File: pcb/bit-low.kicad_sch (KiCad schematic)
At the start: 5 parts, among them Q1 2N7002b, Q2 2N7002b

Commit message: Bit low/high.
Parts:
- renumbered C5 to C23, Q1 to Q909, Q2 to Q910, R1 to R396, R2 to R397
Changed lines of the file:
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@@
     (effects (font (size 1.27 1.27)) (justify left))
   )
-  (symbol (lib_id "power:VCC") (at 184.15 44.45 0) (unit 1)
+  (symbol (lib_id "power:VCC") (at 184.15 44.45 0)
     (in_bom yes) (on_board yes)
-    (property "Reference" "#PWR034" (id 0) (at 184.15 48.26 0)
+    (property "Reference" "#PWR0839" (id 0) (at 184.15 48.26 0)
       (effects (font (size 1.27 1.27)) hide)
     )
@@
     (pin "1")
   )
-  (symbol (lib_id "power:VCC") (at 200.66 40.64 0) (unit 1)
+  (symbol (lib_id "power:VCC") (at 200.66 40.64 0)
     (in_bom yes) (on_board yes)
-    (property "Reference" "#PWR033" (id 0) (at 200.66 44.45 0)
+    (property "Reference" "#PWR0838" (id 0) (at 200.66 44.45 0)
       (effects (font (size 1.27 1.27)) hide)
     )
@@
     (pin "1")
   )
-  (symbol (lib_id "power:VCC") (at 220.98 71.12 0) (unit 1)
+  (symbol (lib_id "power:VCC") (at 220.98 71.12 0)
     (in_bom yes) (on_board yes)
-    (property "Reference" "#PWR036" (id 0) (at 220.98 74.93 0)
+    (property "Reference" "#PWR0841" (id 0) (at 220.98 74.93 0)
       (effects (font (size 1.27 1.27)) hide)
     )
@@
     (pin "1")
   )
-  (symbol (lib_id "power:GND") (at 184.15 52.07 0) (unit 1)
+  (symbol (lib_id "power:GND") (at 184.15 52.07 0)
     (in_bom yes) (on_board yes)
-    (property "Reference" "#PWR035" (id 0) (at 184.15 58.42 0)
+    (property "Reference" "#PWR0840" (id 0) (at 184.15 58.42 0)
       (effects (font (size 1.27 1.27)) hide)
     )
@@
     (pin "1")
   )
-  (symbol (lib_id "power:GND") (at 220.98 109.22 0) (unit 1)
+  (symbol (lib_id "power:GND") (at 220.98 109.22 0)
     (in_bom yes) (on_board yes)
-    (property "Reference" "#PWR037" (id 0) (at 220.98 115.57 0)
+    (property "Reference" "#PWR0842" (id 0) (at 220.98 115.57 0)
       (effects (font (size 1.27 1.27)) hide)
     )
@@
     (pin "1")
   )
-  (symbol (lib_id "Device:R") (at 200.66 44.45 0) (unit 1)
+  (symbol (lib_id "Device:R") (at 200.66 44.45 0)
     (in_bom yes) (on_board yes)
-    (property "Reference" "R1" (id 0) (at 202.438 43.2816 0)
+    (property "Reference" "R396" (id 0) (at 202.438 43.2816 0)
       (effects (font (size 1.27 1.27)) (justify left))
     )
@@
     (pin "2")
   )
-  (symbol (lib_id "Device:R") (at 220.98 74.93 0) (unit 1)
+  (symbol (lib_id "Device:R") (at 220.98 74.93 0)
     (in_bom yes) (on_board yes)
-    (property "Reference" "R2" (id 0) (at 222.758 73.7616 0)
+    (property "Reference" "R397" (id 0) (at 222.758 73.7616 0)
       (effects (font (size 1.27 1.27)) (justify left))
     )
@@
     (pin "2")
   )
-  (symbol (lib_id "Device:C") (at 184.15 48.26 0) (unit 1)
+  (symbol (lib_id "Device:C") (at 184.15 48.26 0)
     (in_bom yes) (on_board yes)
-    (property "Reference" "C5" (id 0) (at 187.071 47.0916 0)
+    (property "Reference" "C23" (id 0) (at 187.071 47.0916 0)
       (effects (font (size 1.27 1.27)) (justify left))
     )
@@
     (pin "2")
   )
-  (symbol (lib_id "Transistor_FET:2N7002") (at 218.44 93.98 0) (unit 1)
+  (symbol (lib_id "Transistor_FET:2N7002") (at 218.44 93.98 0)
     (in_bom yes) (on_board yes)
-    (property "Reference" "Q1" (id 0) (at 223.6724 92.8116 0)
+    (property "Reference" "Q909" (id 0) (at 223.6724 92.8116 0)
       (effects (font (size 1.27 1.27)) (justify left))
     )
@@
     (pin "3")
   )
-  (symbol (lib_id "Transistor_FET:2N7002") (at 218.44 104.14 0) (unit 1)
+  (symbol (lib_id "Transistor_FET:2N7002") (at 218.44 104.14 0)
     (in_bom yes) (on_board yes)
-    (property "Reference" "Q2" (id 0) (at 223.6724 102.9716 0)
+    (property "Reference" "Q910" (id 0) (at 223.6724 102.9716 0)
       (effects (font (size 1.27 1.27)) (justify left))
     )

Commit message: XH/XL.
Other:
- sheet X Register: file xreg.kicad_sch -> xlreg.kicad_sch
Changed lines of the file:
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@@
       (effects (font (size 1.27 1.27)) (justify left bottom))
     )
-    (property "Sheet file" "xreg.kicad_sch" (id 1) (at 110.49 75.4385 0)
+    (property "Sheet file" "xlreg.kicad_sch" (id 1) (at 110.49 75.439 0)
       (effects (font (size 1.27 1.27)) (justify left top))
     )

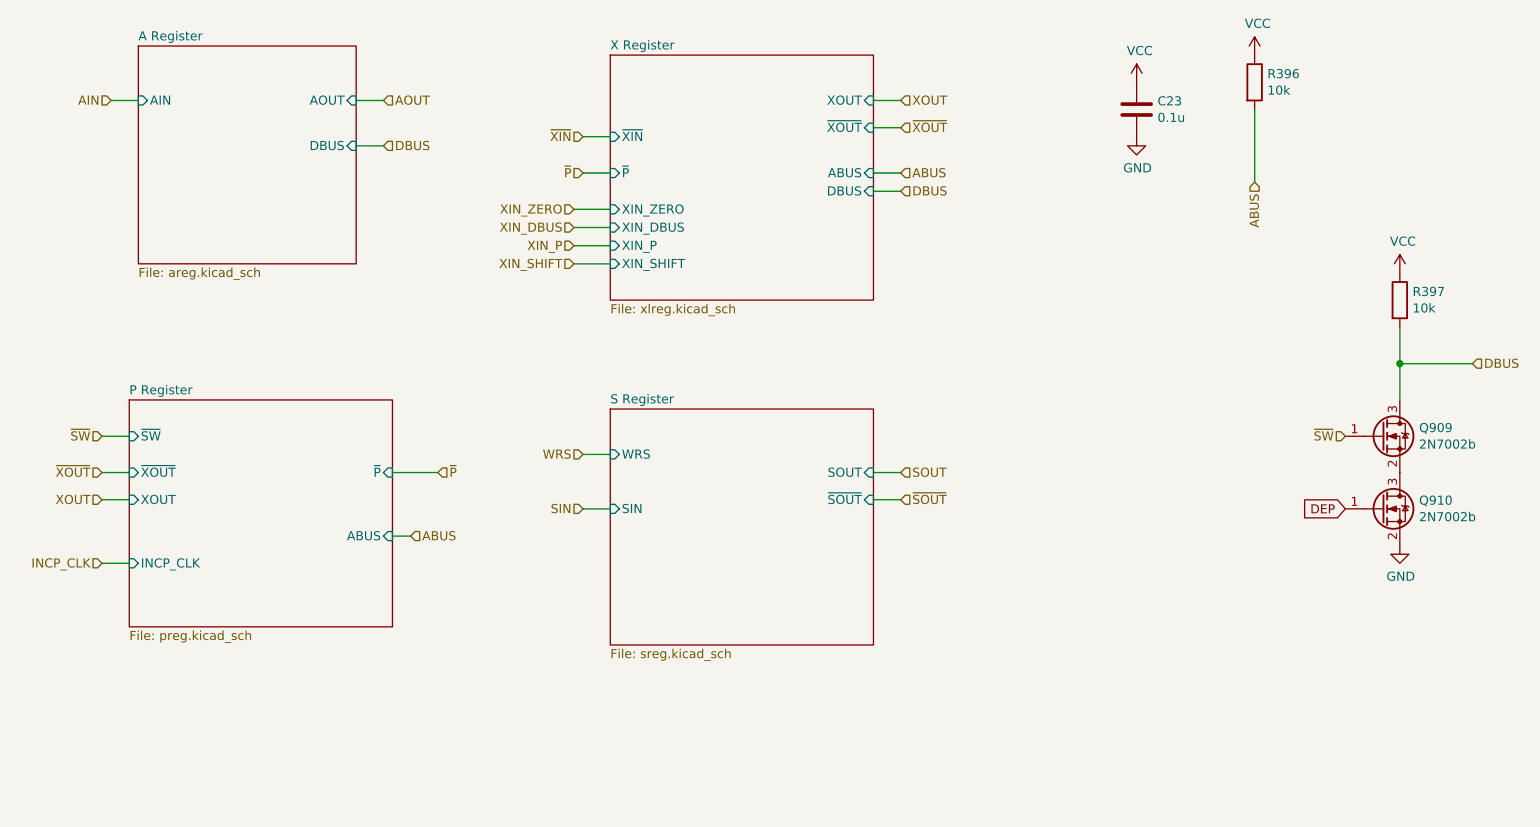
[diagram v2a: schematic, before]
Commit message: Fewer transistors.
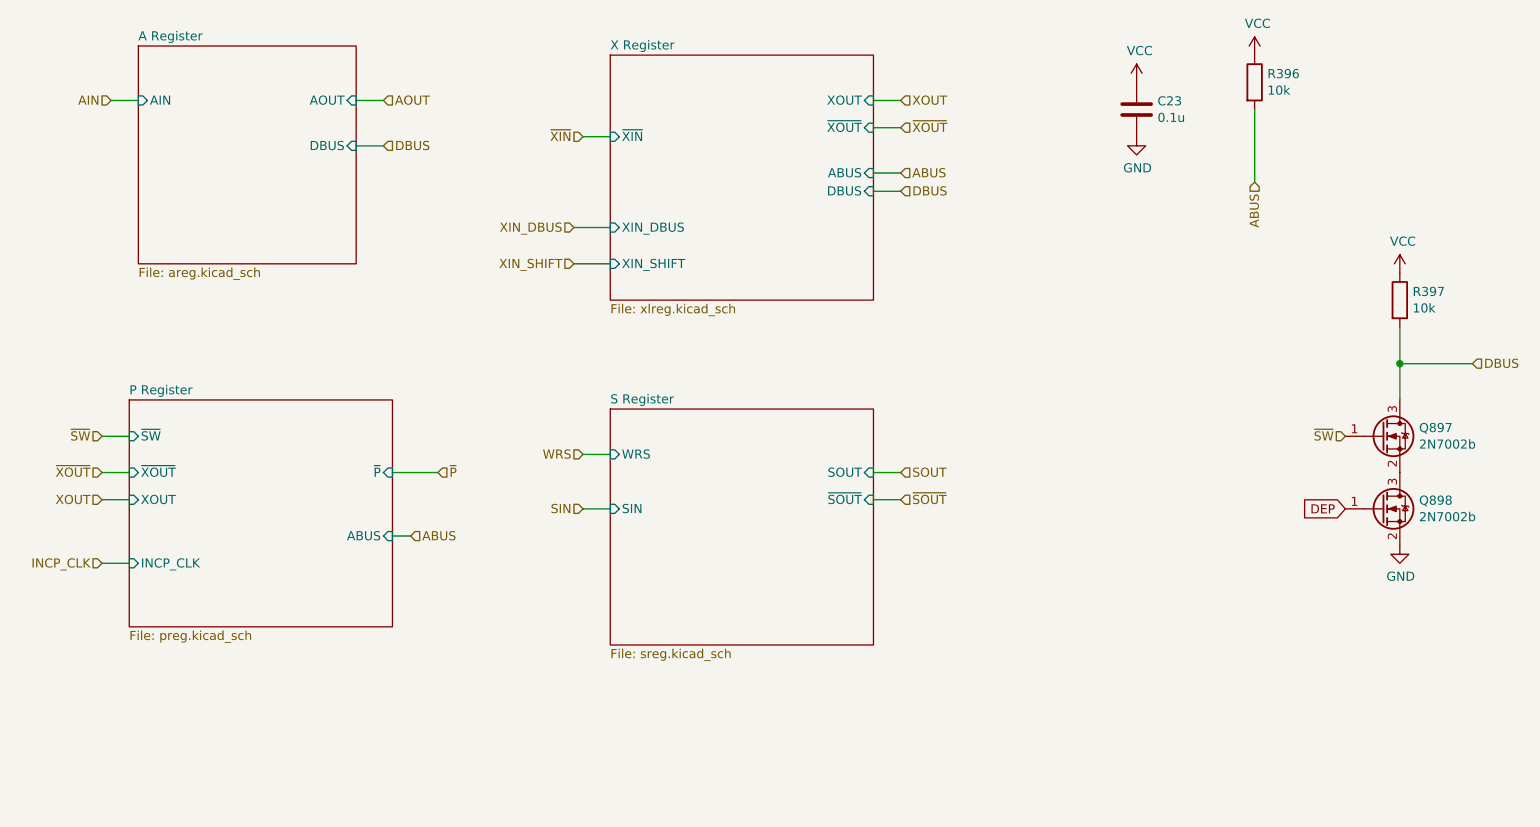
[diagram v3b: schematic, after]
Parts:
- renumbered Q909 to Q897, Q910 to Q898
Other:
- sheet X Register ports: added none; removed XIN_P, XIN_ZERO, ~P
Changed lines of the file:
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@@
-    (stroke (width 0) (type solid) (color 0 0 0 0))
-  )
-  (wire (pts (xy 105.41 62.23) (xy 110.49 62.23))
     (stroke (width 0) (type solid) (color 0 0 0 0))
   )
@@
     (stroke (width 0) (type solid) (color 0 0 0 0))
   )
-  (wire (pts (xy 105.41 67.31) (xy 110.49 67.31))
-    (stroke (width 0) (type solid) (color 0 0 0 0))
-  )
   (wire (pts (xy 105.41 69.85) (xy 110.49 69.85))
     (stroke (width 0) (type solid) (color 0 0 0 0))
@@
     (stroke (width 0) (type solid) (color 0 0 0 0))
   )
-  (wire (pts (xy 106.68 57.15) (xy 110.49 57.15))
-    (stroke (width 0) (type solid) (color 0 0 0 0))
-  )
   (wire (pts (xy 106.68 96.52) (xy 110.49 96.52))
     (stroke (width 0) (type solid) (color 0 0 0 0))
@@
     (effects (font (size 1.27 1.27)) (justify left))
   )
-  (hierarchical_label "XIN_ZERO" (shape input) (at 105.41 62.23 180)
-    (effects (font (size 1.27 1.27)) (justify right))
-  )
   (hierarchical_label "XIN_DBUS" (shape input) (at 105.41 64.77 180)
     (effects (font (size 1.27 1.27)) (justify right))
   )
-  (hierarchical_label "XIN_P" (shape input) (at 105.41 67.31 180)
-    (effects (font (size 1.27 1.27)) (justify right))
-  )
   (hierarchical_label "XIN_SHIFT" (shape input) (at 105.41 69.85 180)
     (effects (font (size 1.27 1.27)) (justify right))
@@
     (effects (font (size 1.27 1.27)) (justify right))
   )
-  (hierarchical_label "~P" (shape input) (at 106.68 57.15 180)
-    (effects (font (size 1.27 1.27)) (justify right))
-  )
   (hierarchical_label "WRS" (shape input) (at 106.68 96.52 180)
     (effects (font (size 1.27 1.27)) (justify right))
@@
   (symbol (lib_id "power:VCC") (at 184.15 44.45 0)
     (in_bom yes) (on_board yes)
-    (property "Reference" "#PWR0839" (id 0) (at 184.15 48.26 0)
+    (property "Reference" "#PWR0817" (id 0) (at 184.15 48.26 0)
       (effects (font (size 1.27 1.27)) hide)
     )
@@
   (symbol (lib_id "power:VCC") (at 200.66 40.64 0)
     (in_bom yes) (on_board yes)
-    (property "Reference" "#PWR0838" (id 0) (at 200.66 44.45 0)
+    (property "Reference" "#PWR0816" (id 0) (at 200.66 44.45 0)
       (effects (font (size 1.27 1.27)) hide)
     )
@@
   (symbol (lib_id "power:VCC") (at 220.98 71.12 0)
     (in_bom yes) (on_board yes)
-    (property "Reference" "#PWR0841" (id 0) (at 220.98 74.93 0)
+    (property "Reference" "#PWR0819" (id 0) (at 220.98 74.93 0)
       (effects (font (size 1.27 1.27)) hide)
     )
@@
   (symbol (lib_id "power:GND") (at 184.15 52.07 0)
     (in_bom yes) (on_board yes)
-    (property "Reference" "#PWR0840" (id 0) (at 184.15 58.42 0)
+    (property "Reference" "#PWR0818" (id 0) (at 184.15 58.42 0)
       (effects (font (size 1.27 1.27)) hide)
     )
@@
   (symbol (lib_id "power:GND") (at 220.98 109.22 0)
     (in_bom yes) (on_board yes)
-    (property "Reference" "#PWR0842" (id 0) (at 220.98 115.57 0)
+    (property "Reference" "#PWR0820" (id 0) (at 220.98 115.57 0)
       (effects (font (size 1.27 1.27)) hide)
     )
@@
   (symbol (lib_id "Transistor_FET:2N7002") (at 218.44 93.98 0)
     (in_bom yes) (on_board yes)
-    (property "Reference" "Q909" (id 0) (at 223.6724 92.8116 0)
+    (property "Reference" "Q897" (id 0) (at 223.6724 92.8116 0)
       (effects (font (size 1.27 1.27)) (justify left))
     )
@@
   (symbol (lib_id "Transistor_FET:2N7002") (at 218.44 104.14 0)
     (in_bom yes) (on_board yes)
-    (property "Reference" "Q910" (id 0) (at 223.6724 102.9716 0)
+    (property "Reference" "Q898" (id 0) (at 223.6724 102.9716 0)
       (effects (font (size 1.27 1.27)) (justify left))
     )
@@
       (effects (font (size 1.27 1.27)) (justify right))
     )
-    (pin "~P" input (at 110.49 57.15 180)
-      (effects (font (size 1.27 1.27)) (justify left))
-    )
     (pin "~XIN" input (at 110.49 52.07 180)
       (effects (font (size 1.27 1.27)) (justify left))
@@
       (effects (font (size 1.27 1.27)) (justify right))
     )
-    (pin "XIN_ZERO" input (at 110.49 62.23 180)
-      (effects (font (size 1.27 1.27)) (justify left))
-    )
     (pin "XIN_DBUS" input (at 110.49 64.77 180)
       (effects (font (size 1.27 1.27)) (justify left))
     )
-    (pin "XIN_P" input (at 110.49 67.31 180)
-      (effects (font (size 1.27 1.27)) (justify left))
-    )

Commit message: New reset.
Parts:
- renumbered C23 to C22, R396 to R395, R397 to R396
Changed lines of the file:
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@@
   (symbol (lib_id "power:VCC") (at 184.15 44.45 0)
     (in_bom yes) (on_board yes)
-    (property "Reference" "#PWR0817" (id 0) (at 184.15 48.26 0)
+    (property "Reference" "#PWR0816" (id 0) (at 184.15 48.26 0)
       (effects (font (size 1.27 1.27)) hide)
     )
@@
   (symbol (lib_id "power:VCC") (at 200.66 40.64 0)
     (in_bom yes) (on_board yes)
-    (property "Reference" "#PWR0816" (id 0) (at 200.66 44.45 0)
+    (property "Reference" "#PWR0815" (id 0) (at 200.66 44.45 0)
       (effects (font (size 1.27 1.27)) hide)
     )
@@
   (symbol (lib_id "power:VCC") (at 220.98 71.12 0)
     (in_bom yes) (on_board yes)
-    (property "Reference" "#PWR0819" (id 0) (at 220.98 74.93 0)
+    (property "Reference" "#PWR0818" (id 0) (at 220.98 74.93 0)
       (effects (font (size 1.27 1.27)) hide)
     )
@@
   (symbol (lib_id "power:GND") (at 184.15 52.07 0)
     (in_bom yes) (on_board yes)
-    (property "Reference" "#PWR0818" (id 0) (at 184.15 58.42 0)
+    (property "Reference" "#PWR0817" (id 0) (at 184.15 58.42 0)
       (effects (font (size 1.27 1.27)) hide)
     )
@@
   (symbol (lib_id "power:GND") (at 220.98 109.22 0)
     (in_bom yes) (on_board yes)
-    (property "Reference" "#PWR0820" (id 0) (at 220.98 115.57 0)
+    (property "Reference" "#PWR0819" (id 0) (at 220.98 115.57 0)
       (effects (font (size 1.27 1.27)) hide)
     )
@@
   (symbol (lib_id "Device:R") (at 200.66 44.45 0)
     (in_bom yes) (on_board yes)
-    (property "Reference" "R396" (id 0) (at 202.438 43.2816 0)
+    (property "Reference" "R395" (id 0) (at 202.438 43.2816 0)
       (effects (font (size 1.27 1.27)) (justify left))
     )
@@
   (symbol (lib_id "Device:R") (at 220.98 74.93 0)
     (in_bom yes) (on_board yes)
-    (property "Reference" "R397" (id 0) (at 222.758 73.7616 0)
+    (property "Reference" "R396" (id 0) (at 222.758 73.7616 0)
       (effects (font (size 1.27 1.27)) (justify left))
     )
@@
   (symbol (lib_id "Device:C") (at 184.15 48.26 0)
     (in_bom yes) (on_board yes)
-    (property "Reference" "C23" (id 0) (at 187.071 47.0916 0)
+    (property "Reference" "C22" (id 0) (at 187.071 47.0916 0)
       (effects (font (size 1.27 1.27)) (justify left))
     )

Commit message: Some fixes.
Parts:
- added Q895: 2N7002b, Package_TO_SOT_SMD:SOT-23, symbol Transistor_FET:2N7002
- renumbered C22 to C26, Q897 to Q893, Q898 to Q894, R395 to R399, R396 to R400
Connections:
- net GND: now also Q895.2 (S)
- new net S Register/CLR: Q895.3 (D)
- new net ~RST: Q895.1 (G)
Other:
- sheet S Register ports: added CLR; removed none
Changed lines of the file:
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@@
+    (stroke (width 0) (type solid) (color 0 0 0 0))
+  )
+  (wire (pts (xy 95.25 111.76) (xy 110.49 111.76))
+    (stroke (width 0) (type solid) (color 0 0 0 0))
+  )
+  (wire (pts (xy 95.25 130.81) (xy 95.25 111.76))
     (stroke (width 0) (type solid) (color 0 0 0 0))
   )
@@
     (stroke (width 0) (type solid) (color 0 0 0 0))
   )
+  (global_label "~RST" (shape input) (at 87.63 135.89 180)
+    (effects (font (size 1.27 1.27)) (justify right))
+    (property "Intersheet References" "${INTERSHEET_REFS}" (id 0) (at 81.7698 135.8106 0)
+      (effects (font (size 1.27 1.27)) (justify right) hide)
+    )
+  )
   (global_label "DEP" (shape input) (at 213.36 104.14 180)
     (effects (font (size 1.27 1.27)) (justify right))
@@
   (symbol (lib_id "power:VCC") (at 184.15 44.45 0)
     (in_bom yes) (on_board yes)
-    (property "Reference" "#PWR0816" (id 0) (at 184.15 48.26 0)
+    (property "Reference" "#PWR0826" (id 0) (at 184.15 48.26 0)
       (effects (font (size 1.27 1.27)) hide)
     )
@@
   (symbol (lib_id "power:VCC") (at 200.66 40.64 0)
     (in_bom yes) (on_board yes)
-    (property "Reference" "#PWR0815" (id 0) (at 200.66 44.45 0)
+    (property "Reference" "#PWR0825" (id 0) (at 200.66 44.45 0)
       (effects (font (size 1.27 1.27)) hide)
     )
@@
   (symbol (lib_id "power:VCC") (at 220.98 71.12 0)
     (in_bom yes) (on_board yes)
-    (property "Reference" "#PWR0818" (id 0) (at 220.98 74.93 0)
+    (property "Reference" "#PWR0828" (id 0) (at 220.98 74.93 0)
       (effects (font (size 1.27 1.27)) hide)
     )
@@
     (pin "1")
   )
+  (symbol (lib_id "power:GND") (at 95.25 140.97 0)
+    (in_bom yes) (on_board yes)
+    (property "Reference" "#PWR0830" (id 0) (at 95.25 147.32 0)
+      (effects (font (size 1.27 1.27)) hide)
+    )
+    (property "Value" "GND" (id 1) (at 95.377 145.3642 0))
+    (property "Footprint" "" (id 2) (at 95.25 140.97 0)
+      (effects (font (size 1.27 1.27)) hide)
+    )
+    (property "Datasheet" "" (id 3) (at 95.25 140.97 0)
+      (effects (font (size 1.27 1.27)) hide)
+    )
+    (pin "1")
+  )
   (symbol (lib_id "power:GND") (at 184.15 52.07 0)
     (in_bom yes) (on_board yes)
-    (property "Reference" "#PWR0817" (id 0) (at 184.15 58.42 0)
+    (property "Reference" "#PWR0827" (id 0) (at 184.15 58.42 0)
       (effects (font (size 1.27 1.27)) hide)
     )
@@
   (symbol (lib_id "power:GND") (at 220.98 109.22 0)
     (in_bom yes) (on_board yes)
-    (property "Reference" "#PWR0819" (id 0) (at 220.98 115.57 0)
+    (property "Reference" "#PWR0829" (id 0) (at 220.98 115.57 0)
       (effects (font (size 1.27 1.27)) hide)
     )
@@
   (symbol (lib_id "Device:R") (at 200.66 44.45 0)
     (in_bom yes) (on_board yes)
-    (property "Reference" "R395" (id 0) (at 202.438 43.2816 0)
+    (property "Reference" "R399" (id 0) (at 202.438 43.2816 0)
       (effects (font (size 1.27 1.27)) (justify left))
     )
@@
   (symbol (lib_id "Device:R") (at 220.98 74.93 0)
     (in_bom yes) (on_board yes)
-    (property "Reference" "R396" (id 0) (at 222.758 73.7616 0)
+    (property "Reference" "R400" (id 0) (at 222.758 73.7616 0)
       (effects (font (size 1.27 1.27)) (justify left))
     )
@@
   (symbol (lib_id "Device:C") (at 184.15 48.26 0)
     (in_bom yes) (on_board yes)
-    (property "Reference" "C22" (id 0) (at 187.071 47.0916 0)
+    (property "Reference" "C26" (id 0) (at 187.071 47.0916 0)
       (effects (font (size 1.27 1.27)) (justify left))
     )
@@
     (pin "2")
   )
+  (symbol (lib_id "Transistor_FET:2N7002") (at 92.71 135.89 0)
+    (in_bom yes) (on_board yes)
+    (property "Reference" "Q895" (id 0) (at 97.9424 134.7216 0)
+      (effects (font (size 1.27 1.27)) (justify left))
+    )
+    (property "Value" "2N7002b" (id 1) (at 97.942 137.033 0)
+      (effects (font (size 1.27 1.27)) (justify left))
+    )
+    (property "Footprint" "Package_TO_SOT_SMD:SOT-23" (id 2) (at 97.79 137.795 0)
+      (effects (font (size 1.27 1.27) italic) (justify left) hide)
+    )
+    (property "Datasheet" "https://www.fairchildsemi.com/datasheets/2N/2N7002.pdf" (id 3) (at 92.71 135.89 0)
+      (effects (font (size 1.27 1.27)) (justify left) hide)
+    )
+    (property "LCSC" "C8545" (id 4) (at 92.71 135.89 0)
+      (effects (font (size 1.27 1.27)) hide)
+    )
+    (pin "1")
+    (pin "2")
+    (pin "3")
+  )
   (symbol (lib_id "Transistor_FET:2N7002") (at 218.44 93.98 0)
     (in_bom yes) (on_board yes)
-    (property "Reference" "Q897" (id 0) (at 223.6724 92.8116 0)
+    (property "Reference" "Q893" (id 0) (at 223.6724 92.8116 0)
       (effects (font (size 1.27 1.27)) (justify left))
     )
@@
   (symbol (lib_id "Transistor_FET:2N7002") (at 218.44 104.14 0)
     (in_bom yes) (on_board yes)
-    (property "Reference" "Q898" (id 0) (at 223.6724 102.9716 0)
+    (property "Reference" "Q894" (id 0) (at 223.6724 102.9716 0)
       (effects (font (size 1.27 1.27)) (justify left))
     )
@@
       (effects (font (size 1.27 1.27)) (justify left))
     )
+    (pin "CLR" input (at 110.49 111.76 180)
+      (effects (font (size 1.27 1.27)) (justify left))
+    )
